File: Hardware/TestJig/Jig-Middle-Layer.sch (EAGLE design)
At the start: 4 parts

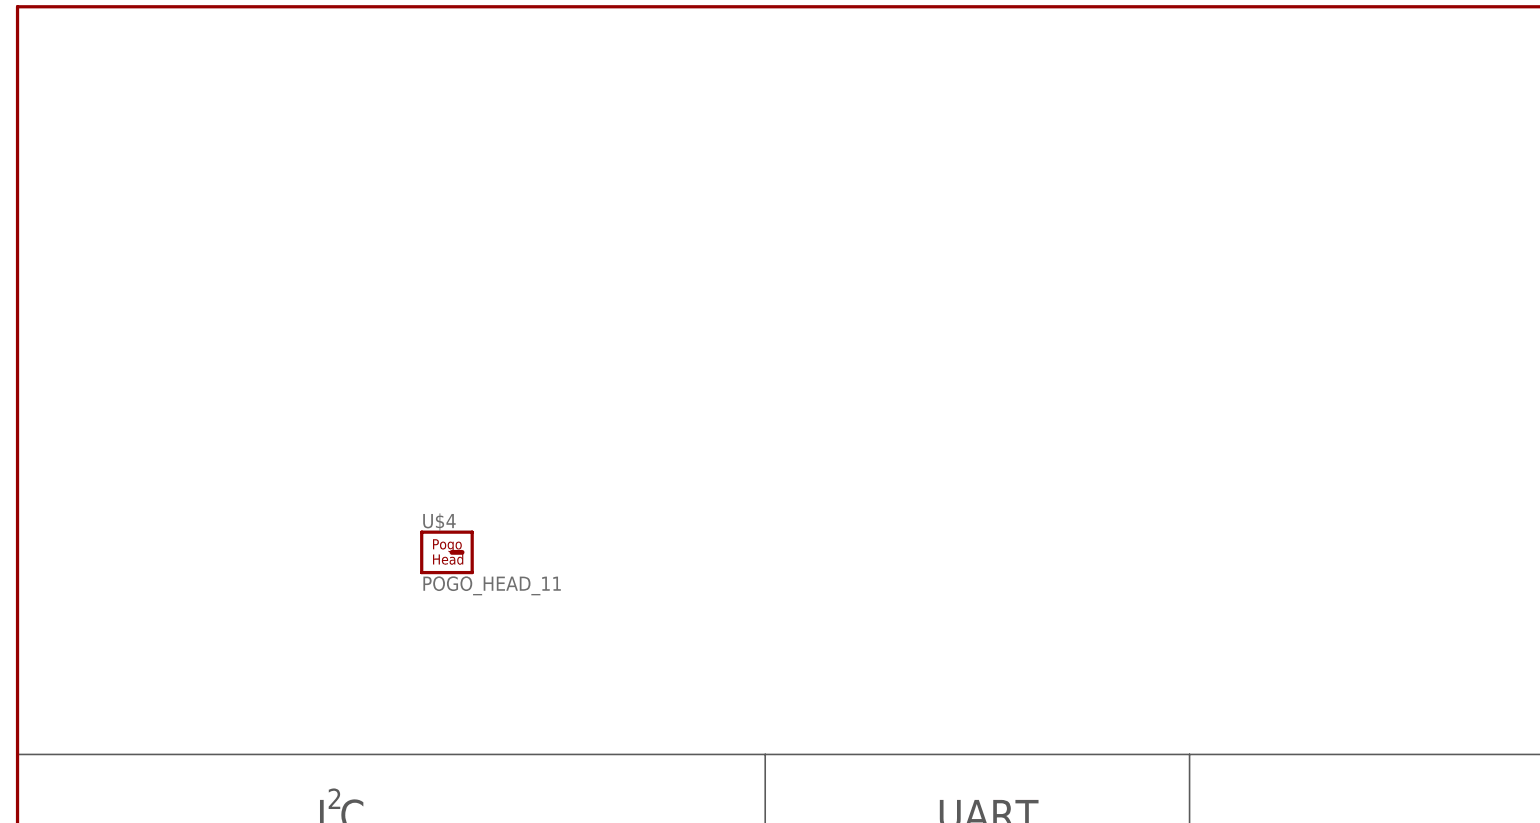
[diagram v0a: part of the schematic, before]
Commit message: fixed white wires on lower layer, added pass throughs for pogo
replaced white wires with bottom traces. 3  traces:  A4, A5, CS

added PTH holes with 1.45mm diameter, giving .15mm clearance of the pogo pin head.

removed cutouts so PCBs can be fabricated
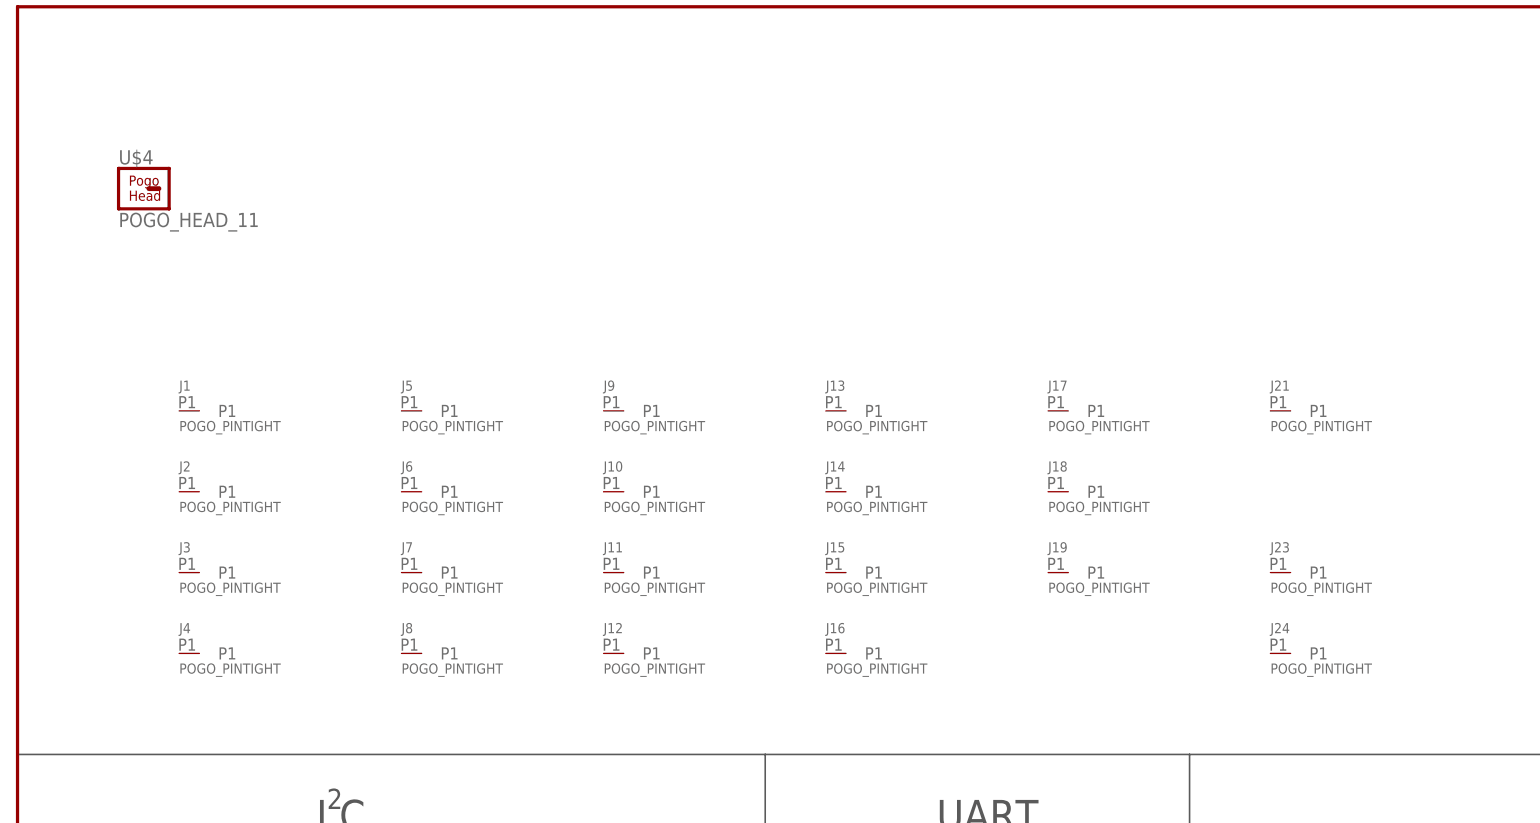
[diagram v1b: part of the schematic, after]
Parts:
- added J1, J10, J11, J12, J13, J14, J15, J16, J17, J18, J19, J2, J21, J23, J24, J3, J4, J5, J6, J7, J8, J9: POGO_PINTIGHT, KevinKuwata_eagle:POGO_PINTIGHT
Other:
- moved on the sheet: U$4
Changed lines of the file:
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@@
 <part name="FRAME1" library="SparkFun-Aesthetics" deviceset="FRAME-LETTER" device=""/>
 <part name="U$4" library="Pogo-Footprints" deviceset="POGO_HEAD_1" device="1"/>
+<part name="J1" library="KevinKuwata_eagle" deviceset="POGO_PIN" device="TIGHT"/>
+<part name="J2" library="KevinKuwata_eagle" deviceset="POGO_PIN" device="TIGHT"/>
+<part name="J3" library="KevinKuwata_eagle" deviceset="POGO_PIN" device="TIGHT"/>
+<part name="J4" library="KevinKuwata_eagle" deviceset="POGO_PIN" device="TIGHT"/>
+<part name="J5" library="KevinKuwata_eagle" deviceset="POGO_PIN" device="TIGHT"/>
+<part name="J6" library="KevinKuwata_eagle" deviceset="POGO_PIN" device="TIGHT"/>
+<part name="J7" library="KevinKuwata_eagle" deviceset="POGO_PIN" device="TIGHT"/>
+<part name="J8" library="KevinKuwata_eagle" deviceset="POGO_PIN" device="TIGHT"/>
+<part name="J9" library="KevinKuwata_eagle" deviceset="POGO_PIN" device="TIGHT"/>
+<part name="J10" library="KevinKuwata_eagle" deviceset="POGO_PIN" device="TIGHT"/>
+<part name="J11" library="KevinKuwata_eagle" deviceset="POGO_PIN" device="TIGHT"/>
+<part name="J12" library="KevinKuwata_eagle" deviceset="POGO_PIN" device="TIGHT"/>
+<part name="J13" library="KevinKuwata_eagle" deviceset="POGO_PIN" device="TIGHT"/>
+<part name="J14" library="KevinKuwata_eagle" deviceset="POGO_PIN" device="TIGHT"/>
+<part name="J15" library="KevinKuwata_eagle" deviceset="POGO_PIN" device="TIGHT"/>
+<part name="J16" library="KevinKuwata_eagle" deviceset="POGO_PIN" device="TIGHT"/>
+<part name="J17" library="KevinKuwata_eagle" deviceset="POGO_PIN" device="TIGHT"/>
+<part name="J18" library="KevinKuwata_eagle" deviceset="POGO_PIN" device="TIGHT"/>
+<part name="J19" library="KevinKuwata_eagle" deviceset="POGO_PIN" device="TIGHT"/>
+<part name="J21" library="KevinKuwata_eagle" deviceset="POGO_PIN" device="TIGHT"/>
+<part name="J23" library="KevinKuwata_eagle" deviceset="POGO_PIN" device="TIGHT"/>
+<part name="J24" library="KevinKuwata_eagle" deviceset="POGO_PIN" device="TIGHT"/>
 </parts>
 <sheets>
@@
 <instance part="FRAME1" gate="G$1" x="0" y="0"/>
 <instance part="FRAME1" gate="V" x="147.32" y="0"/>
-<instance part="U$4" gate="G$1" x="53.34" y="116.84"/>
+<instance part="U$4" gate="G$1" x="15.24" y="162.56"/>
+<instance part="J1" gate="J1" x="22.86" y="134.62"/>
+<instance part="J2" gate="J1" x="22.86" y="124.46"/>
+<instance part="J3" gate="J1" x="22.86" y="114.3"/>
+<instance part="J4" gate="J1" x="22.86" y="104.14"/>
+<instance part="J5" gate="J1" x="50.8" y="134.62"/>
+<instance part="J6" gate="J1" x="50.8" y="124.46"/>
+<instance part="J7" gate="J1" x="50.8" y="114.3"/>
+<instance part="J8" gate="J1" x="50.8" y="104.14"/>
+<instance part="J9" gate="J1" x="76.2" y="134.62"/>
+<instance part="J10" gate="J1" x="76.2" y="124.46"/>
+<instance part="J11" gate="J1" x="76.2" y="114.3"/>
+<instance part="J12" gate="J1" x="76.2" y="104.14"/>
+<instance part="J13" gate="J1" x="104.14" y="134.62"/>
+<instance part="J14" gate="J1" x="104.14" y="124.46"/>
+<instance part="J15" gate="J1" x="104.14" y="114.3"/>
+<instance part="J16" gate="J1" x="104.14" y="104.14"/>
+<instance part="J17" gate="J1" x="132.08" y="134.62"/>
+<instance part="J18" gate="J1" x="132.08" y="124.46"/>
+<instance part="J19" gate="J1" x="132.08" y="114.3"/>
+<instance part="J21" gate="J1" x="160.02" y="134.62"/>
+<instance part="J23" gate="J1" x="160.02" y="114.3"/>
+<instance part="J24" gate="J1" x="160.02" y="104.14"/>
 </instances>
 <busses>

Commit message: Tweaked testjig middle and top layers
middle layer changes:
-changed holes for the pogopins to pup up through from pads to actual "holes" in eagle file. removed pads from sch and board.
-set hole size to 0.055 inch diameter for optimal lazer cutting in acrylic.

top layer changes:
-tightened up frame to huge product dimensions with 0.016 inch gap.
-added corner cutouts
-added "lift-out" cutout on the side, for easier product removal

Also note, bumped outer dimensions on both middle and top to allow for more strength around the corner standoff holes. Previous deisgn would probably crack if cut in acrylic with lazer.
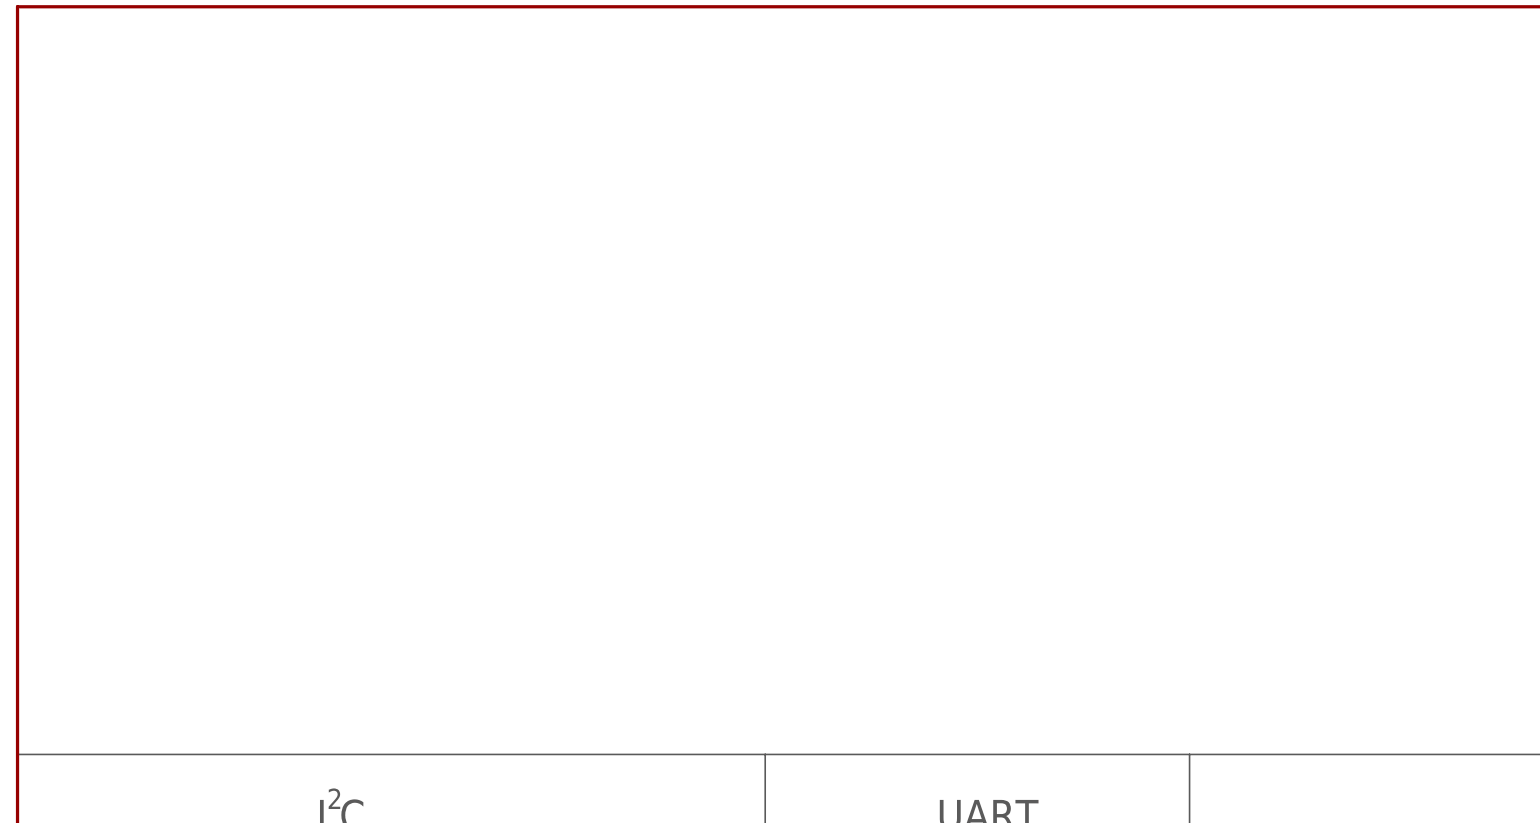
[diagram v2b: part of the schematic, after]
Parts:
- removed J1, J10, J11, J12, J13, J14, J15, J16, J17, J18, J19, J2, J21, J23, J24, J3, J4, J5, J6, J7, J8, J9: POGO_PINTIGHT, KevinKuwata_eagle:POGO_PINTIGHT
- removed U$4: POGO_HEAD_11, Pogo-Footprints:POGO_HEAD_11
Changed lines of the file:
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@@
 <?xml version="1.0" encoding="utf-8"?>
 <!DOCTYPE eagle SYSTEM "eagle.dtd">
-<eagle version="7.7.0">
+<eagle version="7.6.0">
 <drawing>
 <settings>
@@
 <part name="JP4" library="SparkFun" deviceset="STAND-OFF" device=""/>
 <part name="FRAME1" library="SparkFun-Aesthetics" deviceset="FRAME-LETTER" device=""/>
-<part name="U$4" library="Pogo-Footprints" deviceset="POGO_HEAD_1" device="1"/>
-<part name="J1" library="KevinKuwata_eagle" deviceset="POGO_PIN" device="TIGHT"/>
-<part name="J2" library="KevinKuwata_eagle" deviceset="POGO_PIN" device="TIGHT"/>
-<part name="J3" library="KevinKuwata_eagle" deviceset="POGO_PIN" device="TIGHT"/>
-<part name="J4" library="KevinKuwata_eagle" deviceset="POGO_PIN" device="TIGHT"/>
-<part name="J5" library="KevinKuwata_eagle" deviceset="POGO_PIN" device="TIGHT"/>
-<part name="J6" library="KevinKuwata_eagle" deviceset="POGO_PIN" device="TIGHT"/>
-<part name="J7" library="KevinKuwata_eagle" deviceset="POGO_PIN" device="TIGHT"/>
-<part name="J8" library="KevinKuwata_eagle" deviceset="POGO_PIN" device="TIGHT"/>
-<part name="J9" library="KevinKuwata_eagle" deviceset="POGO_PIN" device="TIGHT"/>
-<part name="J10" library="KevinKuwata_eagle" deviceset="POGO_PIN" device="TIGHT"/>
-<part name="J11" library="KevinKuwata_eagle" deviceset="POGO_PIN" device="TIGHT"/>
-<part name="J12" library="KevinKuwata_eagle" deviceset="POGO_PIN" device="TIGHT"/>
-<part name="J13" library="KevinKuwata_eagle" deviceset="POGO_PIN" device="TIGHT"/>
-<part name="J14" library="KevinKuwata_eagle" deviceset="POGO_PIN" device="TIGHT"/>
-<part name="J15" library="KevinKuwata_eagle" deviceset="POGO_PIN" device="TIGHT"/>
-<part name="J16" library="KevinKuwata_eagle" deviceset="POGO_PIN" device="TIGHT"/>
-<part name="J17" library="KevinKuwata_eagle" deviceset="POGO_PIN" device="TIGHT"/>
-<part name="J18" library="KevinKuwata_eagle" deviceset="POGO_PIN" device="TIGHT"/>
-<part name="J19" library="KevinKuwata_eagle" deviceset="POGO_PIN" device="TIGHT"/>
-<part name="J21" library="KevinKuwata_eagle" deviceset="POGO_PIN" device="TIGHT"/>
-<part name="J23" library="KevinKuwata_eagle" deviceset="POGO_PIN" device="TIGHT"/>
-<part name="J24" library="KevinKuwata_eagle" deviceset="POGO_PIN" device="TIGHT"/>
 </parts>
 <sheets>
@@
 <instance part="FRAME1" gate="G$1" x="0" y="0"/>
 <instance part="FRAME1" gate="V" x="147.32" y="0"/>
-<instance part="U$4" gate="G$1" x="15.24" y="162.56"/>
-<instance part="J1" gate="J1" x="22.86" y="134.62"/>
-<instance part="J2" gate="J1" x="22.86" y="124.46"/>
-<instance part="J3" gate="J1" x="22.86" y="114.3"/>
-<instance part="J4" gate="J1" x="22.86" y="104.14"/>
-<instance part="J5" gate="J1" x="50.8" y="134.62"/>
-<instance part="J6" gate="J1" x="50.8" y="124.46"/>
-<instance part="J7" gate="J1" x="50.8" y="114.3"/>
-<instance part="J8" gate="J1" x="50.8" y="104.14"/>
-<instance part="J9" gate="J1" x="76.2" y="134.62"/>
-<instance part="J10" gate="J1" x="76.2" y="124.46"/>
-<instance part="J11" gate="J1" x="76.2" y="114.3"/>
-<instance part="J12" gate="J1" x="76.2" y="104.14"/>
-<instance part="J13" gate="J1" x="104.14" y="134.62"/>
-<instance part="J14" gate="J1" x="104.14" y="124.46"/>
-<instance part="J15" gate="J1" x="104.14" y="114.3"/>
-<instance part="J16" gate="J1" x="104.14" y="104.14"/>
-<instance part="J17" gate="J1" x="132.08" y="134.62"/>
-<instance part="J18" gate="J1" x="132.08" y="124.46"/>
-<instance part="J19" gate="J1" x="132.08" y="114.3"/>
-<instance part="J21" gate="J1" x="160.02" y="134.62"/>
-<instance part="J23" gate="J1" x="160.02" y="114.3"/>
-<instance part="J24" gate="J1" x="160.02" y="104.14"/>
 </instances>
 <busses>
